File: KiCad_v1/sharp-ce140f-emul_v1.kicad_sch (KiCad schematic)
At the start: 29 parts, among them J1 Conn_01x01, J2 Micro_SD_Card_Det, J3 Conn_01x15, J4 Conn_01x15, J5 Conn_01x01, J6 Conn_01x01, J7 Conn_01x01, J8 Sharp PC 11-pin, U1 NUCLEO-L053R8, U2 NUCLEO-L432KC

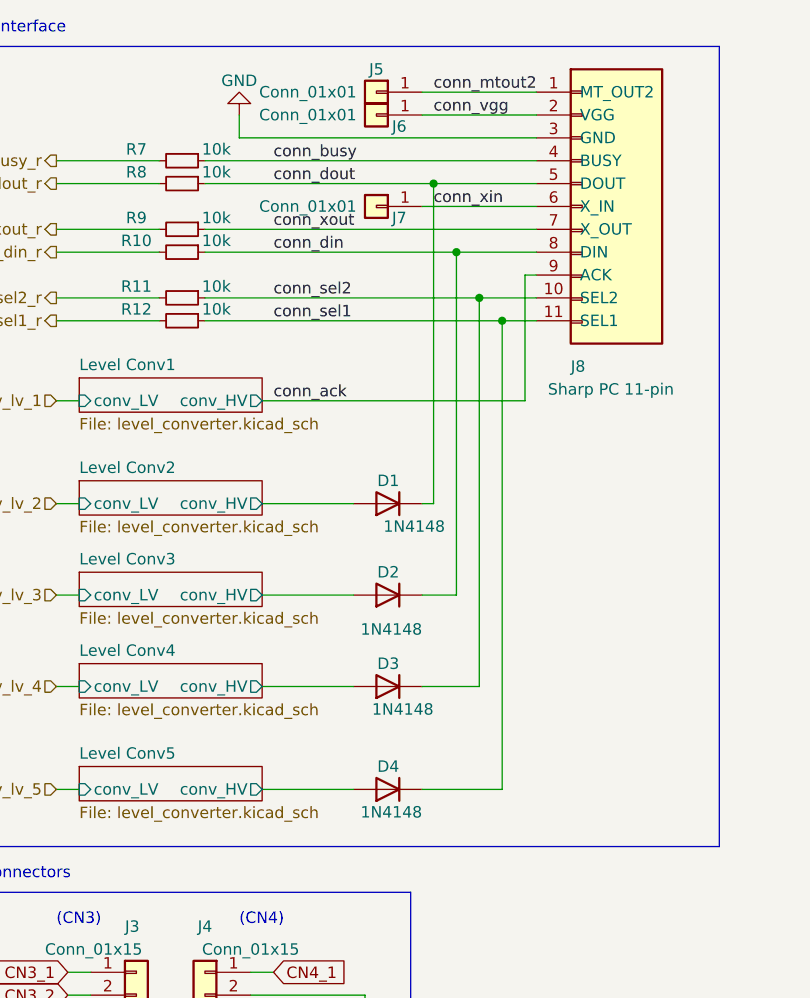
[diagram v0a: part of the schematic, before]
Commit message: Level converter changed to 74LV1T34
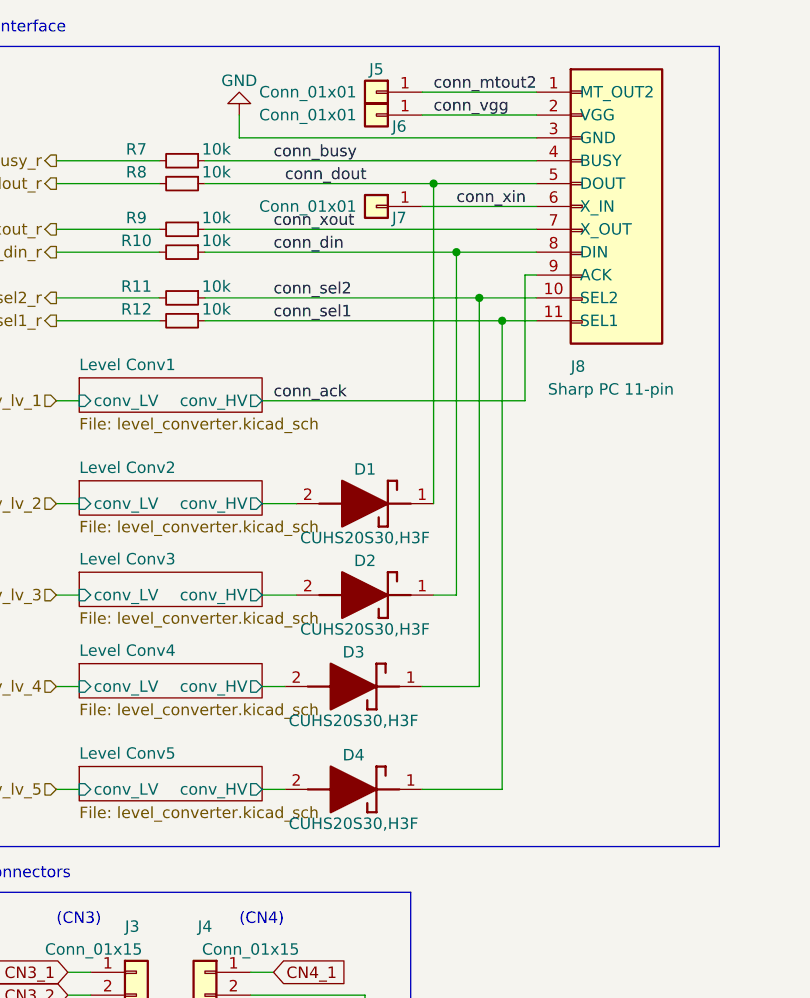
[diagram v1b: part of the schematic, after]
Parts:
- removed D1, D2, D3, D4: 1N4148, Diode_SMD:D_SOD-323_HandSoldering, symbol Device:D
- added D1, D2, D3, D4: CUHS20S30,H3F, CUHS20S40H3F, symbol sharp-ce140f-emul:CUHS20S30,H3F
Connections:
- net Level Conv2/conv_HV: now also D1.2 (A)
- net Level Conv3/conv_HV: now also D2.2 (A)
- net Level Conv4/conv_HV: now also D3.2 (A)
- net Level Conv5/conv_HV: now also D4.2 (A)
- net conn_din: now also D2.1 (K)
- net conn_dout: now also D1.1 (K); no longer J7.1 (Pin_1), J8.6 (X_IN)
- net conn_sel1: now also D4.1 (K)
- net conn_sel2: now also D3.1 (K)
- new net conn_xin: J7.1 (Pin_1), J8.6 (X_IN)
